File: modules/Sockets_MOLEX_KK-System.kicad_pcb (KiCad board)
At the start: 2 copper layers, 13 parts

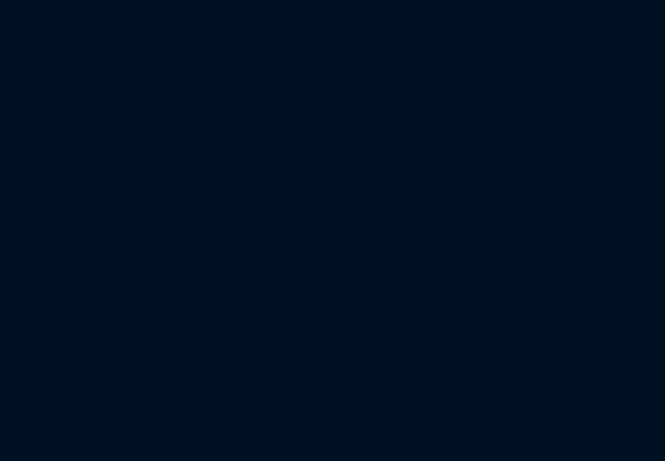
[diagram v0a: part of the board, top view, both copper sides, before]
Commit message: Added 47054 Molex header
Added Molex header for pc pwm fans
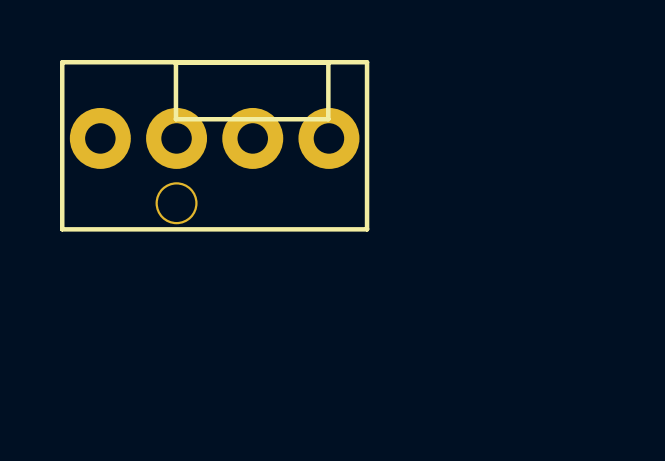
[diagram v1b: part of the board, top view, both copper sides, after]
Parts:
- added ?: 47053-1000, Socket_MOLEX_KK_47053-1000, F.Cu at (0.00, 0.00)
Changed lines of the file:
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@@
     (add_net "")
   )
+  (module Socket_MOLEX_KK_47053-1000 (layer F.Cu)
+  (fp_text value 47053-1000 (at 0 -5.08) (layer F.Fab)
+    (effects (font (size 1 1) (thickness 0.15)))
+  )
+    (fp_line (start -1.29 -0.64) (end 3.79 -0.64) (layer F.SilkS) (width 0.15))
+    (fp_line (start 3.79 -0.64) (end 3.79 -2.54) (layer F.SilkS) (width 0.15))
+    (fp_line (start 3.79 -2.54) (end -1.29 -2.54) (layer F.SilkS) (width 0.15))
+    (fp_line (start -1.29 -0.64) (end -1.29 -2.54) (layer F.SilkS) (width 0.15))
+    (fp_line (start -5.08 -2.54) (end -5.08 3.03) (layer F.SilkS) (width 0.15))
+    (fp_line (start -5.08 3.03) (end 5.08 3.03) (layer F.SilkS) (width 0.15))
+    (fp_line (start 5.08 3.03) (end 5.08 -2.54) (layer F.SilkS) (width 0.15))
+    (fp_line (start 5.08 -2.54) (end -5.08 -2.54) (layer F.SilkS) (width 0.15))
+    (pad 1 thru_hole circle (at -3.81 0) (size 2.032 2.032) (drill 1.016) (layers B.Cu F.SilkS B.Mask))
+    (pad 2 thru_hole circle (at -1.27 0) (size 2.032 2.032) (drill 1.016) (layers B.Cu F.SilkS B.Mask))
+    (pad 3 thru_hole circle (at 1.27 0) (size 2.032 2.032) (drill 1.016) (layers B.Cu F.SilkS B.Mask))
+    (pad 4 thru_hole circle (at 3.81 0) (size 2.032 2.032) (drill 1.016) (layers B.Cu F.SilkS B.Mask))
+    (pad 5 thru_hole circle (at -1.27 2.16) (size 1.4 1.4) (drill 1.25) (layers *.Cu *.Mask F.SilkS))
+ )
   (module Gauge_100mm_Type2_SilkScreenTop_RevA_Date22Jun2010 (layer Vorderseite)
     (at 94 143)
